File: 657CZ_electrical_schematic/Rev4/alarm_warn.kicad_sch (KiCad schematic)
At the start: 13 parts, among them SW23 LANDING LIGHT TAXI, SW24 Desc

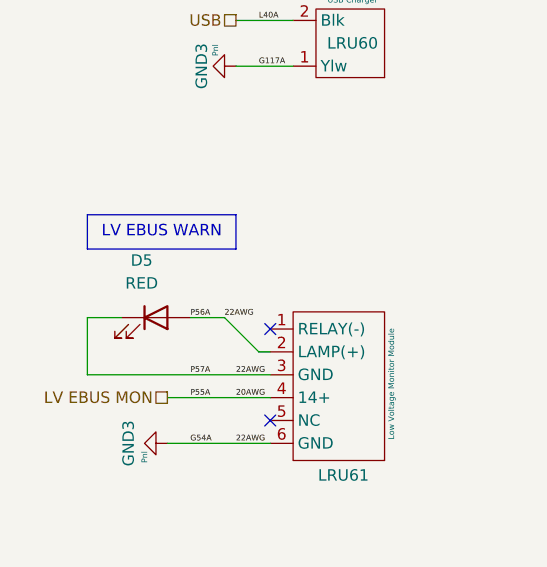
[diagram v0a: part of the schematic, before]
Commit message: added Locations for outstanding components
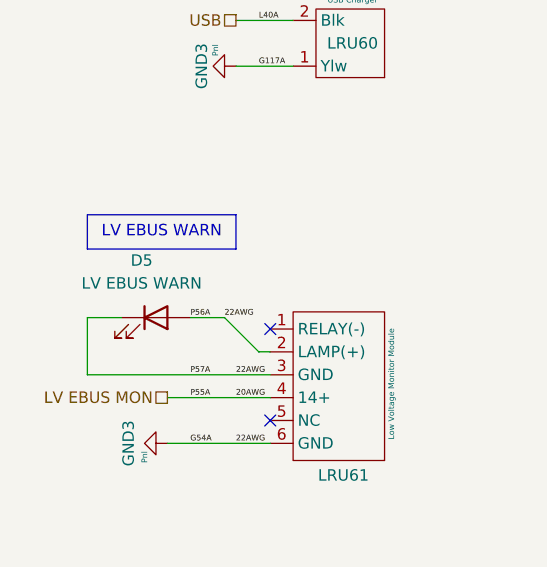
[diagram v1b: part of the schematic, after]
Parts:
- D5: value RED -> LV EBUS WARN; LocLoad (0,0,0)L1 -> (41.3,22.9,6.)L1
- L23: value ~ -> INTR LGHT LED FWD; LocLoad (0,0,0)L2 -> (41,19,20)L2
- L6: value ~ -> INTR LED AFT; LocLoad (0,0,0)L2 -> (124,21,-19)L2
- L7: LocLoad (0,0,0)L4 -> (3.9,11.3,2.3)L4
- L9: LocLoad (0,0,0)L4 -> (3.9,11.3,-2.3)L4
- LRU60: LocLoad (0,0,0)L5 -> (40,21,-16)L5
- LRU61: LocLoad (0,0,0)L1 -> (40,23,6)L1
- LRU81: LocLoad (0,0,0)L4 -> (40,23,-5)L4
- LRU85: LocLoad (0,0,0)L3 -> (163.1,17.7,168.8)L3
- LRU89: LocLoad (0,0,0)L3 -> (163.1,17.7,-168.8)L3
- R7: value R_Variable_US -> INTR LGHT DIM; LocLoad (0,0,0)R4 -> (41.3,22.9,-4.6)R4
- SW23: LocLoad (0,0,0)R20 -> (41.3,24.9,-1.3)R20
- SW24: value Desc -> NAV+STRB; LocLoad (0,0,0)R20 -> (41.3,24.9,-.3)R20
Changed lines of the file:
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@@
 			)
 		)
-		(property "LocLoad" "(0,0,0)R20"
+		(property "LocLoad" "(41.3,24.9,-1.3)R20"
 			(at 224.79 77.47 0)
 			(effects
@@
 			)
 		)
-		(property "LocLoad" "(0,0,0)L4"
+		(property "LocLoad" "(3.9,11.3,-2.3)L4"
 			(at 247.65 83.82 0)
 			(effects
@@
 			)
 		)
-		(property "LocLoad" "(0,0,0)L3"
+		(property "LocLoad" "(163.1,17.7,-168.8)L3"
 			(at 257.81 127 0)
 			(effects
@@
 			)
 		)
-		(property "Value" "~"
+		(property "Value" "INTR LED AFT"
 			(at 237.49 27.94 0)
 			(effects
@@
 			)
 		)
-		(property "LocLoad" "(0,0,0)L2"
+		(property "LocLoad" "(124,21,-19)L2"
 			(at 237.49 33.02 0)
 			(effects
@@
 			)
 		)
-		(property "LocLoad" "(0,0,0)L4"
+		(property "LocLoad" "(40,23,-5)L4"
 			(at 223.52 48.26 0)
 			(effects
@@
 			)
 		)
-		(property "Value" "~"
+		(property "Value" "INTR LGHT LED FWD"
 			(at 237.49 15.24 0)
 			(effects
@@
 			)
 		)
-		(property "LocLoad" "(0,0,0)L2"
+		(property "LocLoad" "(41,19,20)L2"
 			(at 237.49 20.32 0)
 			(effects
@@
 			)
 		)
-		(property "LocLoad" "(0,0,0)L3"
+		(property "LocLoad" "(163.1,17.7,168.8)L3"
 			(at 257.81 110.49 0)
 			(effects
@@
 			)
 		)
-		(property "LocLoad" "(0,0,0)L1"
+		(property "LocLoad" "(40,23,6)L1"
 			(at 180.34 115.57 0)
 			(effects
@@
 			)
 		)
-		(property "Value" "RED"
+		(property "Value" "LV EBUS WARN"
 			(at 158.4325 104.14 0)
 			(effects
@@
 			)
 		)
-		(property "LocLoad" "(0,0,0)L1"
+		(property "LocLoad" "(41.3,22.9,6.)L1"
 			(at 160.02 107.95 0)
 			(effects
@@
 			)
 		)
-		(property "LocLoad" "(0,0,0)L5"
+		(property "LocLoad" "(40,21,-16)L5"
 			(at 180.34 77.47 0)
 			(effects
@@
 			)
 		)
-		(property "Value" "R_Variable_US"
+		(property "Value" "INTR LGHT DIM"
 			(at 204.5081 26.67 90)
 			(effects
@@
 			)
 		)
-		(property "LocLoad" "(0,0,0)R4"
+		(property "LocLoad" "(41.3,22.9,-4.6)R4"
 			(at 204.47 30.48 90)
 			(effects
@@
 			)
 		)
-		(property "Value" "Desc"
+		(property "Value" "NAV+STRB"
 			(at 227.33 110.998 0)
 			(do_not_autoplace yes)
@@
 			)
 		)
-		(property "LocLoad" "(0,0,0)R20"
+		(property "LocLoad" "(41.3,24.9,-.3)R20"
 			(at 227.33 119.38 0)
 			(effects
@@
 			)
 		)
-		(property "LocLoad" "(0,0,0)L4"
+		(property "LocLoad" "(3.9,11.3,2.3)L4"
 			(at 240.03 78.74 0)
 			(effects
